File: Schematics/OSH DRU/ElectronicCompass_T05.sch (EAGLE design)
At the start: 67 parts, among them Q1 FDN360P, Q2 FDN360P, Q3 FDN360P, Q4 FDN360P, Q5 BC817-16LT1SMD, Q6 BC817-16LT1SMD, U1 ATMEGA32U4, X1 USBSMD, Y1 16MHz

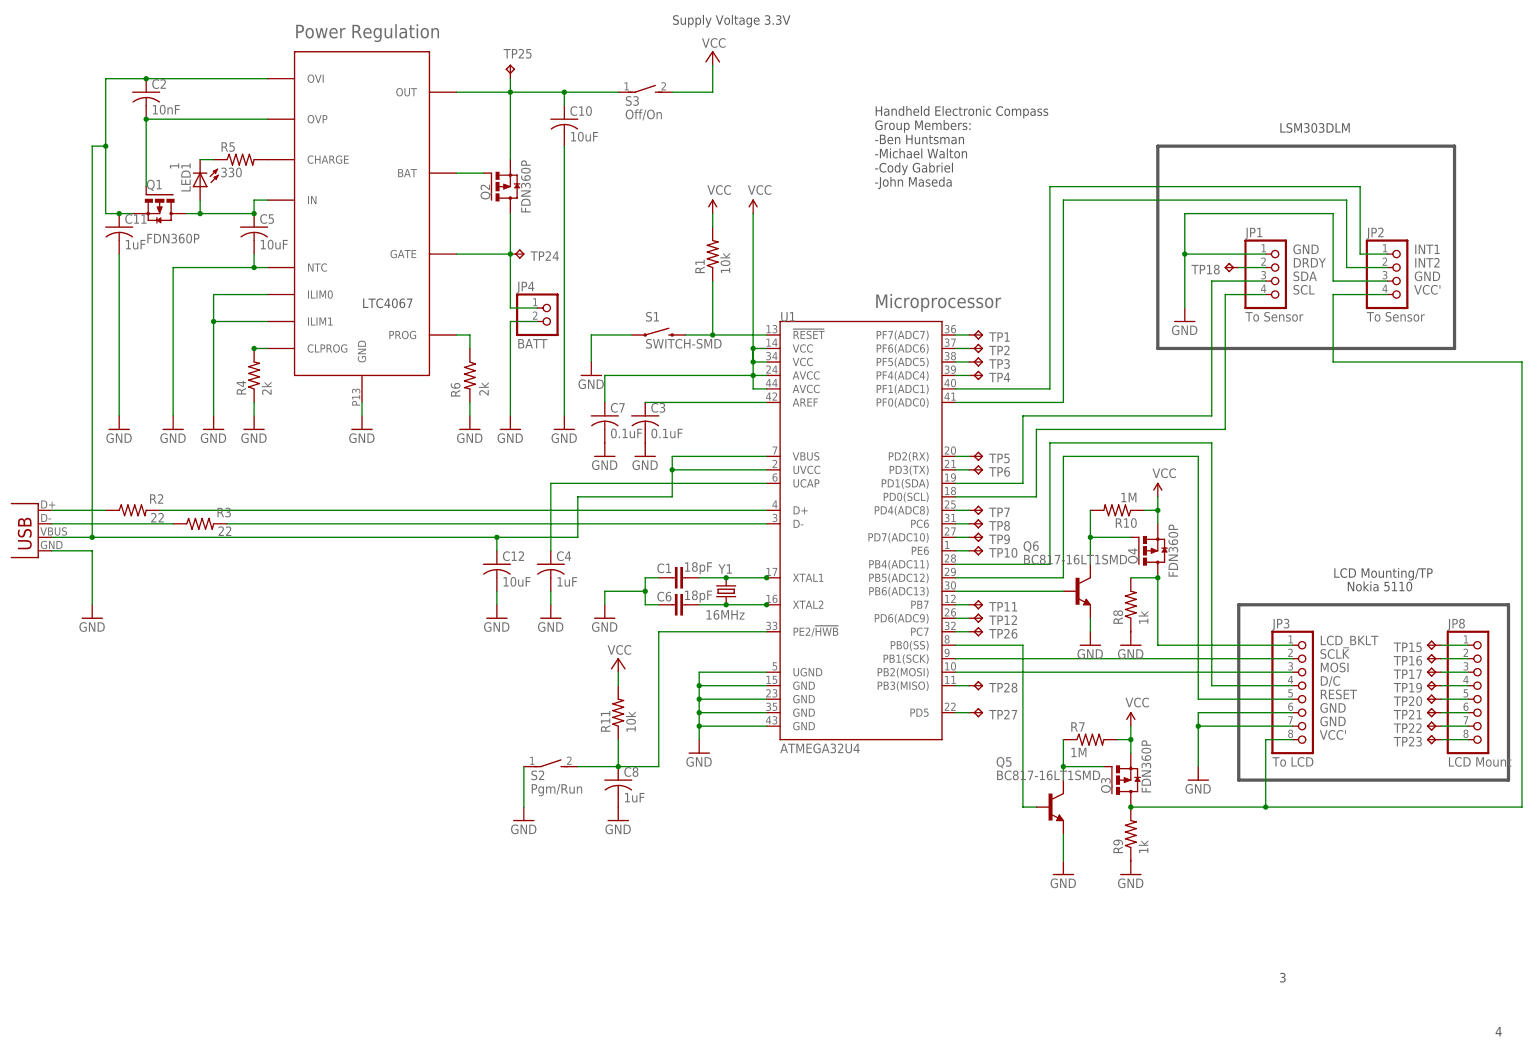
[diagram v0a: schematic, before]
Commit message: Fixed PMIC pins and GPIO switches
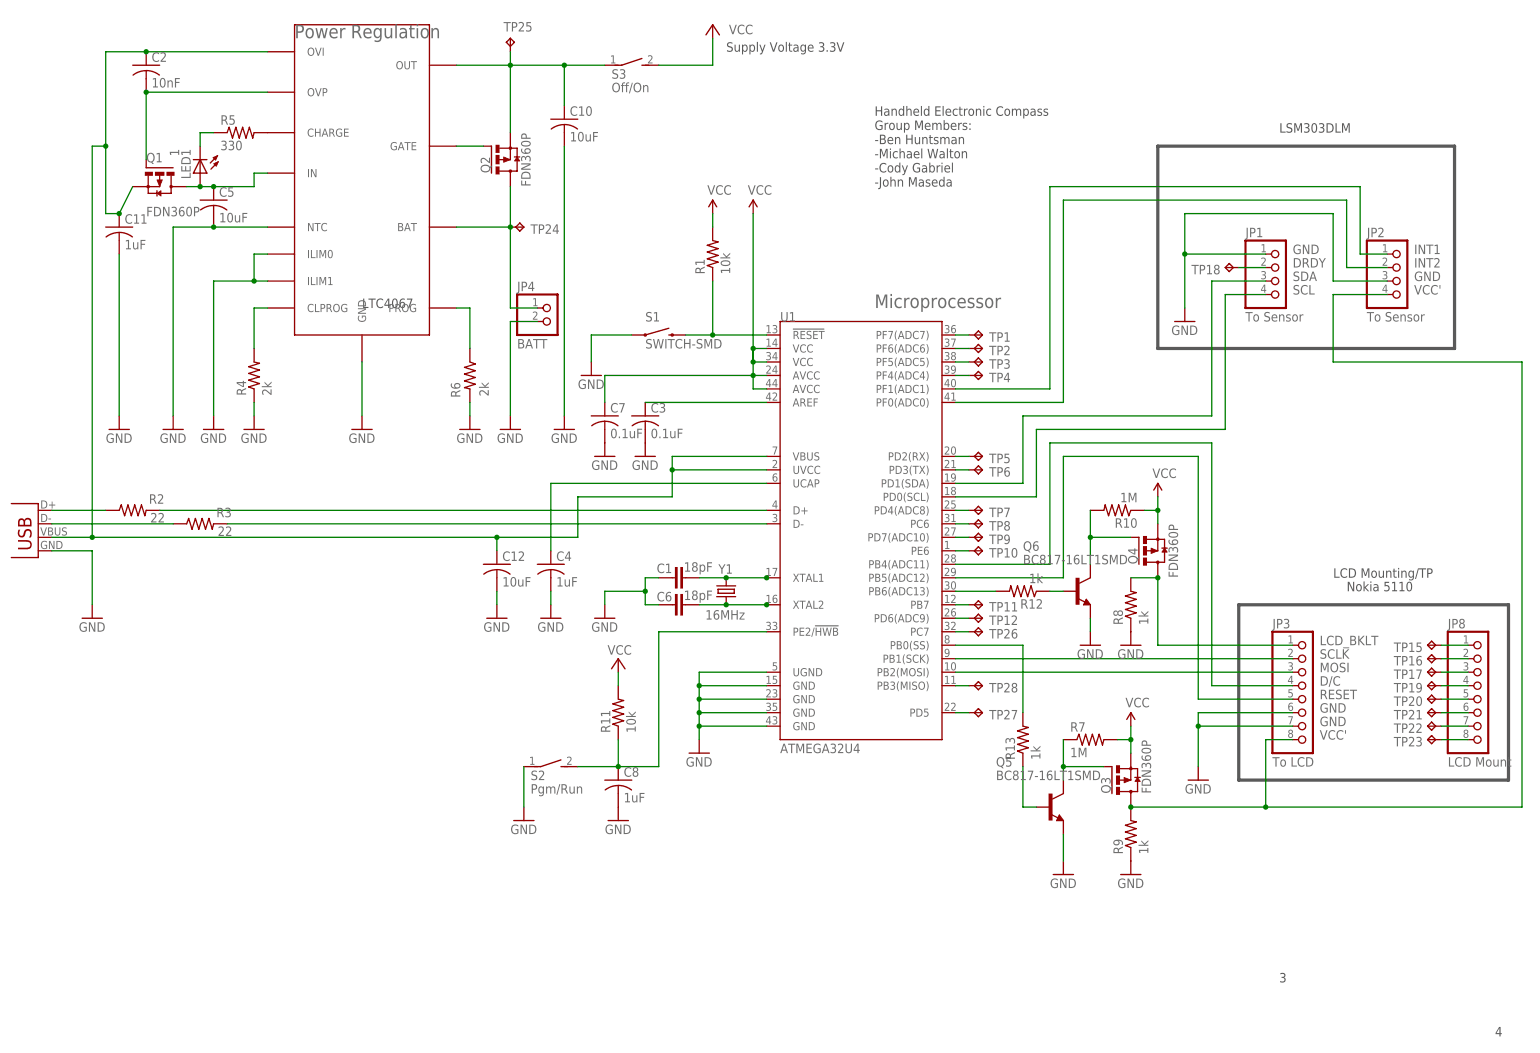
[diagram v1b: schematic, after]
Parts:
- added R12: 1k, rcl:R-US_M0805
- added R13: 1k, resistor:R-US_M0805
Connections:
- new net N$46: Q2.G, U$1.GATE
- new net N$47: Q5.B, R13.1
- net N$16: now also R12.2, U1.PB6(ADC13); no longer Q2.G, U$1.BAT
- net N$37: now also R13.2; no longer Q5.B
- net N$44: now also R12.1; no longer U1.PB6(ADC13)
- net N$5: now also U$1.BAT; no longer U$1.GATE
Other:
- moved on the sheet: C2, C5, LED1, Q1, Q2, R5, S3, TP24, TP25

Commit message: board layout complete
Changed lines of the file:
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@@
 <part name="TP27" library="testpad" deviceset="TP" device="TP06R"/>
 <part name="TP28" library="testpad" deviceset="TP" device="TP06R"/>
-<part name="U$1" library="LTC4067" deviceset="LTC4067" device=""/>
 <part name="Q4" library="transistor-power" deviceset="FDN360P" device=""/>
 <part name="Q1" library="transistor-power" deviceset="FDN360P" device=""/>
@@
 <part name="R12" library="rcl" deviceset="R-US_" device="M0805" value="1k"/>
 <part name="R13" library="resistor" deviceset="R-US_" device="M0805" value="1k"/>
+<part name="U$1" library="LTC4067" deviceset="LTC4067" device=""/>
 </parts>
 <sheets>
@@
 <attribute name="TP_SIGNAL_NAME" x="166.37" y="-44.45" size="1.778" layer="97" rot="R270"/>
 </instance>
-<instance part="U$1" gate="G$1" x="50.8" y="45.72" rot="R270"/>
 <instance part="Q4" gate="G$1" x="198.12" y="-17.78" smashed="yes">
 <attribute name="NAME" x="196.85" y="-20.32" size="1.778" layer="95" rot="R90"/>
@@
 <attribute name="VALUE" x="178.562" y="-57.15" size="1.778" layer="96" rot="R90"/>
 </instance>
+<instance part="U$1" gate="G$1" x="50.8" y="50.8" rot="R270"/>
 </instances>
 <busses>
@@
 <segment>
 <pinref part="GND9" gate="1" pin="GND"/>
+<wire x1="50.8" y1="7.62" x2="50.8" y2="15.24" width="0.1524" layer="91"/>
 <pinref part="U$1" gate="G$1" pin="GND"/>
-<wire x1="50.8" y1="7.62" x2="50.8" y2="17.78" width="0.1524" layer="91"/>
-</segment>
-<segment>
-<wire x1="22.86" y1="7.62" x2="22.86" y2="33.02" width="0.1524" layer="91"/>
+<wire x1="50.8" y1="15.24" x2="50.8" y2="17.78" width="0.1524" layer="91"/>
+<junction x="50.8" y="15.24"/>
+</segment>
+<segment>
+<wire x1="22.86" y1="7.62" x2="22.86" y2="30.48" width="0.1524" layer="91"/>
 <pinref part="GND6" gate="1" pin="GND"/>
+<wire x1="33.02" y1="35.56" x2="30.48" y2="35.56" width="0.1524" layer="91"/>
+<wire x1="30.48" y1="35.56" x2="30.48" y2="30.48" width="0.1524" layer="91"/>
+<wire x1="30.48" y1="30.48" x2="22.86" y2="30.48" width="0.1524" layer="91"/>
+<wire x1="33.02" y1="30.48" x2="30.48" y2="30.48" width="0.1524" layer="91"/>
+<junction x="30.48" y="30.48"/>
+<pinref part="U$1" gate="G$1" pin="ILIM1"/>
 <pinref part="U$1" gate="G$1" pin="ILIM0"/>
-<wire x1="33.02" y1="38.1" x2="30.48" y2="38.1" width="0.1524" layer="91"/>
-<wire x1="30.48" y1="38.1" x2="30.48" y2="33.02" width="0.1524" layer="91"/>
-<wire x1="30.48" y1="33.02" x2="22.86" y2="33.02" width="0.1524" layer="91"/>
-<pinref part="U$1" gate="G$1" pin="ILIM1"/>
-<wire x1="33.02" y1="33.02" x2="30.48" y2="33.02" width="0.1524" layer="91"/>
-<junction x="30.48" y="33.02"/>
-</segment>
-<segment>
-<pinref part="U$1" gate="G$1" pin="NTC"/>
-<wire x1="33.02" y1="43.18" x2="22.86" y2="43.18" width="0.1524" layer="91"/>
+</segment>
+<segment>
+<wire x1="33.02" y1="40.64" x2="30.48" y2="40.64" width="0.1524" layer="91"/>
+<wire x1="30.48" y1="40.64" x2="30.48" y2="43.18" width="0.1524" layer="91"/>
+<wire x1="30.48" y1="43.18" x2="22.86" y2="43.18" width="0.1524" layer="91"/>
 <pinref part="GND18" gate="1" pin="GND"/>
 <wire x1="22.86" y1="43.18" x2="15.24" y2="43.18" width="0.1524" layer="91"/>
@@
 <pinref part="C5" gate="G$1" pin="2"/>
 <junction x="22.86" y="43.18"/>
+<pinref part="U$1" gate="G$1" pin="NTC"/>
 </segment>
 <segment>
@@
 <junction x="20.32" y="50.8"/>
 <pinref part="Q1" gate="G$1" pin="D"/>
-<pinref part="U$1" gate="G$1" pin="IN"/>
 <wire x1="33.02" y1="53.34" x2="30.48" y2="53.34" width="0.1524" layer="91"/>
 <wire x1="30.48" y1="53.34" x2="30.48" y2="50.8" width="0.1524" layer="91"/>
 <wire x1="30.48" y1="50.8" x2="22.86" y2="50.8" width="0.1524" layer="91"/>
 <junction x="22.86" y="50.8"/>
+<pinref part="U$1" gate="G$1" pin="IN"/>
 </segment>
 </net>
@@
 <pinref part="C2" gate="G$1" pin="2"/>
 <junction x="10.16" y="68.58"/>
+<pinref part="Q1" gate="G$1" pin="G"/>
 <pinref part="U$1" gate="G$1" pin="OVP"/>
-<pinref part="Q1" gate="G$1" pin="G"/>
 </segment>
 </net>
@@
 <wire x1="0" y1="58.42" x2="0" y2="-15.24" width="0.1524" layer="91"/>
 <junction x="2.54" y="58.42"/>
-<pinref part="U$1" gate="G$1" pin="OVI"/>
 <pinref part="Q1" gate="G$1" pin="S"/>
 <pinref part="U1" gate="G$1" pin="VBUS"/>
@@
 <junction x="76.2" y="-15.24"/>
 <junction x="0" y="-15.24"/>
+<pinref part="U$1" gate="G$1" pin="OVI"/>
 </segment>
 </net>
@@
 <pinref part="JP4" gate="G$1" pin="1"/>
 <wire x1="78.74" y1="27.94" x2="83.82" y2="27.94" width="0.1524" layer="91"/>
+<wire x1="68.58" y1="43.18" x2="78.74" y2="43.18" width="0.1524" layer="91"/>
 <pinref part="U$1" gate="G$1" pin="BAT"/>
-<wire x1="68.58" y1="43.18" x2="78.74" y2="43.18" width="0.1524" layer="91"/>
 </segment>
 </net>
@@
 <wire x1="88.9" y1="73.66" x2="96.52" y2="73.66" width="0.1524" layer="91"/>
 <junction x="88.9" y="73.66"/>
+<wire x1="68.58" y1="73.66" x2="78.74" y2="73.66" width="0.1524" layer="91"/>
 <pinref part="U$1" gate="G$1" pin="OUT"/>
-<wire x1="68.58" y1="73.66" x2="78.74" y2="73.66" width="0.1524" layer="91"/>
 </segment>
 </net>
@@
 <pinref part="TP28" gate="G$1" pin="TP"/>
 <wire x1="165.1" y1="-43.18" x2="162.56" y2="-43.18" width="0.1524" layer="91"/>
-</segment>
-</net>
-<net name="N$7" class="0">
-<segment>
-<pinref part="R5" gate="G$1" pin="2"/>
-<pinref part="U$1" gate="G$1" pin="CHARGE"/>
 </segment>
 </net>
@@
 <segment>
 <pinref part="R6" gate="G$1" pin="1"/>
-<pinref part="U$1" gate="G$1" pin="PROG"/>
 <wire x1="68.58" y1="27.94" x2="71.12" y2="27.94" width="0.1524" layer="91"/>
 <wire x1="71.12" y1="27.94" x2="71.12" y2="20.32" width="0.1524" layer="91"/>
+<pinref part="U$1" gate="G$1" pin="PROG"/>
 </segment>
 </net>
@@
 <net name="N$4" class="0">
 <segment>
+<wire x1="33.02" y1="25.4" x2="30.48" y2="25.4" width="0.1524" layer="91"/>
+<pinref part="R4" gate="G$1" pin="2"/>
+<wire x1="30.48" y1="20.32" x2="30.48" y2="25.4" width="0.1524" layer="91"/>
 <pinref part="U$1" gate="G$1" pin="CLPROG"/>
-<wire x1="33.02" y1="27.94" x2="30.48" y2="27.94" width="0.1524" layer="91"/>
-<pinref part="R4" gate="G$1" pin="2"/>
-<wire x1="30.48" y1="20.32" x2="30.48" y2="27.94" width="0.1524" layer="91"/>
 </segment>
 </net>
 <net name="N$46" class="0">
 <segment>
-<pinref part="U$1" gate="G$1" pin="GATE"/>
 <pinref part="Q2" gate="G$1" pin="G"/>
 <wire x1="68.58" y1="58.42" x2="73.66" y2="58.42" width="0.1524" layer="91"/>
+<pinref part="U$1" gate="G$1" pin="GATE"/>
 </segment>
 </net>
@@
 </segment>
 </net>
+<net name="N$7" class="0">
+<segment>
+<pinref part="R5" gate="G$1" pin="2"/>
+<pinref part="U$1" gate="G$1" pin="CHARGE"/>
+</segment>
+</net>

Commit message: s-screen layout update
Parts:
- renumbered U$1 to U2
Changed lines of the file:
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@@
 <part name="R12" library="rcl" deviceset="R-US_" device="M0805" value="1k"/>
 <part name="R13" library="resistor" deviceset="R-US_" device="M0805" value="1k"/>
-<part name="U$1" library="LTC4067" deviceset="LTC4067" device=""/>
+<part name="U2" library="LTC4067" deviceset="LTC4067" device=""/>
 </parts>
 <sheets>
@@
 <attribute name="VALUE" x="178.562" y="-57.15" size="1.778" layer="96" rot="R90"/>
 </instance>
-<instance part="U$1" gate="G$1" x="50.8" y="50.8" rot="R270"/>
+<instance part="U2" gate="G$1" x="50.8" y="50.8" rot="R270"/>
 </instances>
 <busses>
@@
 <pinref part="GND9" gate="1" pin="GND"/>
 <wire x1="50.8" y1="7.62" x2="50.8" y2="15.24" width="0.1524" layer="91"/>
-<pinref part="U$1" gate="G$1" pin="GND"/>
+<pinref part="U2" gate="G$1" pin="GND"/>
 <wire x1="50.8" y1="15.24" x2="50.8" y2="17.78" width="0.1524" layer="91"/>
 <junction x="50.8" y="15.24"/>
@@
 <wire x1="33.02" y1="30.48" x2="30.48" y2="30.48" width="0.1524" layer="91"/>
 <junction x="30.48" y="30.48"/>
-<pinref part="U$1" gate="G$1" pin="ILIM1"/>
-<pinref part="U$1" gate="G$1" pin="ILIM0"/>
+<pinref part="U2" gate="G$1" pin="ILIM1"/>
+<pinref part="U2" gate="G$1" pin="ILIM0"/>
 </segment>
 <segment>
@@
 <pinref part="C5" gate="G$1" pin="2"/>
 <junction x="22.86" y="43.18"/>
-<pinref part="U$1" gate="G$1" pin="NTC"/>
+<pinref part="U2" gate="G$1" pin="NTC"/>
 </segment>
 <segment>
@@
 <wire x1="30.48" y1="50.8" x2="22.86" y2="50.8" width="0.1524" layer="91"/>
 <junction x="22.86" y="50.8"/>
-<pinref part="U$1" gate="G$1" pin="IN"/>
+<pinref part="U2" gate="G$1" pin="IN"/>
 </segment>
 </net>
@@
 <junction x="10.16" y="68.58"/>
 <pinref part="Q1" gate="G$1" pin="G"/>
-<pinref part="U$1" gate="G$1" pin="OVP"/>
+<pinref part="U2" gate="G$1" pin="OVP"/>
 </segment>
 </net>
@@
 <junction x="76.2" y="-15.24"/>
 <junction x="0" y="-15.24"/>
-<pinref part="U$1" gate="G$1" pin="OVI"/>
+<pinref part="U2" gate="G$1" pin="OVI"/>
 </segment>
 </net>
@@
 <wire x1="78.74" y1="27.94" x2="83.82" y2="27.94" width="0.1524" layer="91"/>
 <wire x1="68.58" y1="43.18" x2="78.74" y2="43.18" width="0.1524" layer="91"/>
-<pinref part="U$1" gate="G$1" pin="BAT"/>
+<pinref part="U2" gate="G$1" pin="BAT"/>
 </segment>
 </net>
@@
 <junction x="88.9" y="73.66"/>
 <wire x1="68.58" y1="73.66" x2="78.74" y2="73.66" width="0.1524" layer="91"/>
-<pinref part="U$1" gate="G$1" pin="OUT"/>
+<pinref part="U2" gate="G$1" pin="OUT"/>
 </segment>
 </net>
@@
 <wire x1="68.58" y1="27.94" x2="71.12" y2="27.94" width="0.1524" layer="91"/>
 <wire x1="71.12" y1="27.94" x2="71.12" y2="20.32" width="0.1524" layer="91"/>
-<pinref part="U$1" gate="G$1" pin="PROG"/>
+<pinref part="U2" gate="G$1" pin="PROG"/>
 </segment>
 </net>
@@
 <pinref part="R4" gate="G$1" pin="2"/>
 <wire x1="30.48" y1="20.32" x2="30.48" y2="25.4" width="0.1524" layer="91"/>
-<pinref part="U$1" gate="G$1" pin="CLPROG"/>
+<pinref part="U2" gate="G$1" pin="CLPROG"/>
 </segment>
 </net>
@@
 <pinref part="Q2" gate="G$1" pin="G"/>
 <wire x1="68.58" y1="58.42" x2="73.66" y2="58.42" width="0.1524" layer="91"/>
-<pinref part="U$1" gate="G$1" pin="GATE"/>
+<pinref part="U2" gate="G$1" pin="GATE"/>
 </segment>
 </net>
@@
 <segment>
 <pinref part="R5" gate="G$1" pin="2"/>
-<pinref part="U$1" gate="G$1" pin="CHARGE"/>
-</segment>
-</net>
+<pinref part="U2" gate="G$1" pin="CHARGE"/>
+</segment>
+</net>

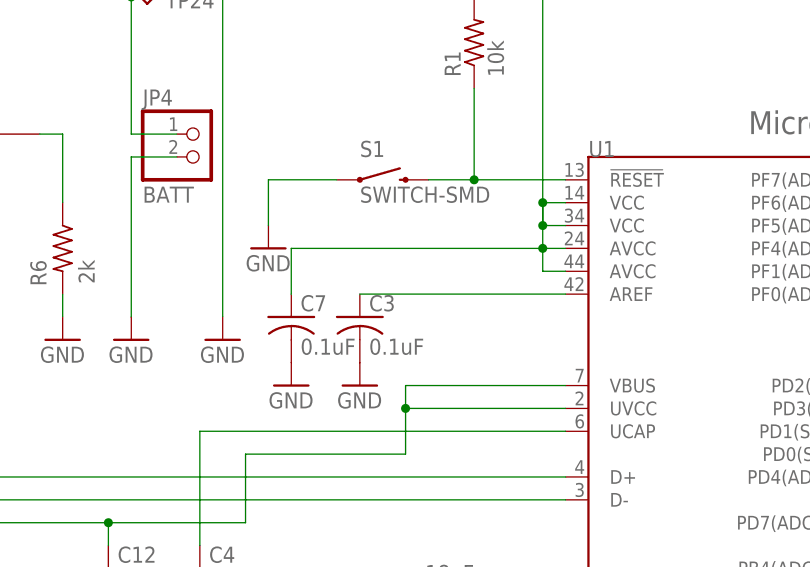
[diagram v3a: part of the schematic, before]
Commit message: Removed capacitor
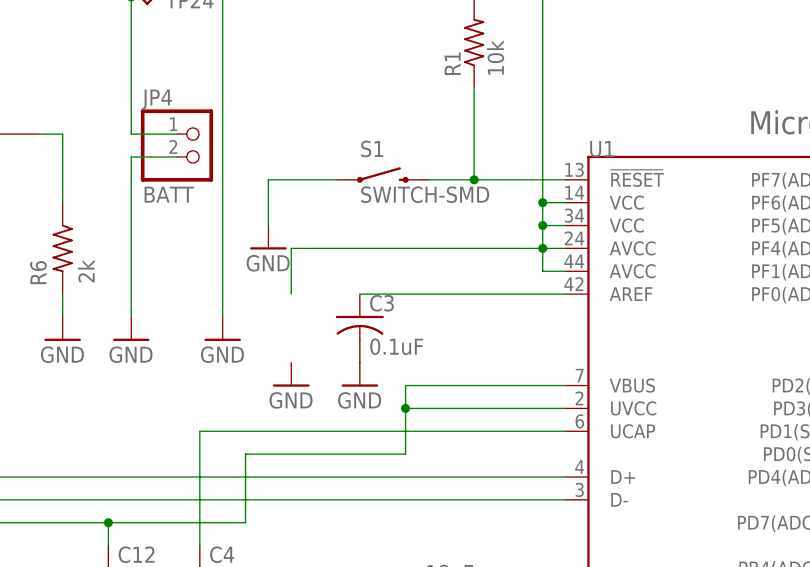
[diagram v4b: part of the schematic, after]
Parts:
- removed C7: 0.1uF, rcl:C-USC0805
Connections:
- net GND: no longer C7.2
- net VCC: no longer C7.1
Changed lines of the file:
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@@
 <part name="GND3" library="SparkFun" deviceset="GND" device=""/>
 <part name="GND6" library="supply1" deviceset="GND" device=""/>
-<part name="C7" library="rcl" deviceset="C-US" device="C0805" value="0.1uF"/>
 <part name="R7" library="resistor" deviceset="R-US_" device="M0805" value="1M"/>
 <part name="R9" library="resistor" deviceset="R-US_" device="M0805" value="1k"/>
@@
 <instance part="GND3" gate="1" x="96.52" y="-30.48"/>
 <instance part="GND6" gate="1" x="22.86" y="5.08"/>
-<instance part="C7" gate="G$1" x="96.52" y="7.62"/>
 <instance part="R7" gate="G$1" x="187.96" y="-53.34" smashed="yes">
 <attribute name="NAME" x="184.15" y="-51.8414" size="1.778" layer="95"/>
@@
 </segment>
 <segment>
-<pinref part="C7" gate="G$1" pin="2"/>
-<pinref part="GND22" gate="1" pin="GND"/>
-</segment>
-<segment>
 <wire x1="81.28" y1="-58.42" x2="81.28" y2="-66.04" width="0.1524" layer="91"/>
 <pinref part="GND23" gate="1" pin="GND"/>
@@
 <wire x1="127" y1="20.32" x2="124.46" y2="20.32" width="0.1524" layer="91"/>
 <wire x1="127" y1="17.78" x2="124.46" y2="17.78" width="0.1524" layer="91"/>
-<wire x1="124.46" y1="17.78" x2="124.46" y2="20.32" width="0.1524" layer="91"/>
 <wire x1="127" y1="15.24" x2="124.46" y2="15.24" width="0.1524" layer="91"/>
 <wire x1="124.46" y1="15.24" x2="124.46" y2="17.78" width="0.1524" layer="91"/>
@@
 <pinref part="P+2" gate="1" pin="VCC"/>
 <wire x1="124.46" y1="45.72" x2="124.46" y2="20.32" width="0.1524" layer="91"/>
-<pinref part="C7" gate="G$1" pin="1"/>
 <wire x1="124.46" y1="20.32" x2="124.46" y2="17.78" width="0.1524" layer="91"/>
 <wire x1="124.46" y1="15.24" x2="96.52" y2="15.24" width="0.1524" layer="91"/>
